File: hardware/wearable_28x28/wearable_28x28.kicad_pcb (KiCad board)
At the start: 4 copper layers, 61.2 x 61.2 mm, 784 parts

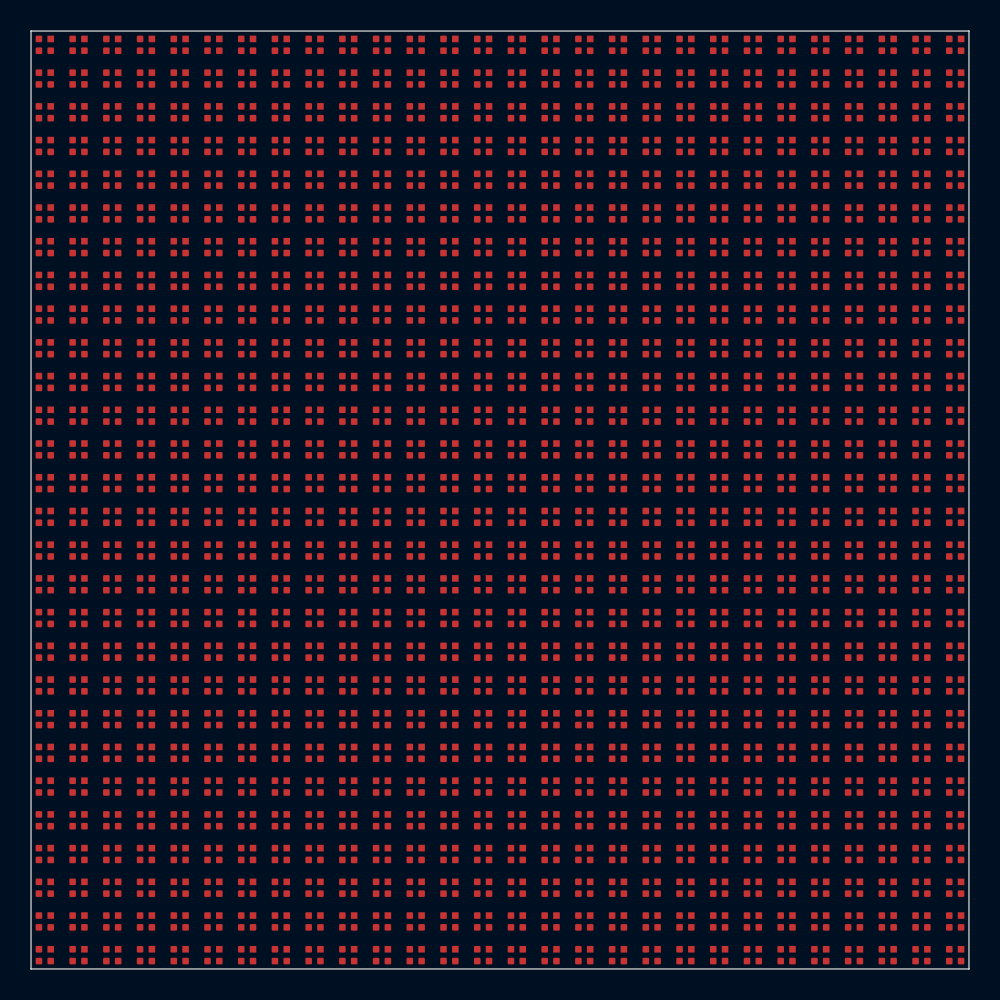
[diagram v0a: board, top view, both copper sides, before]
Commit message: Promote verified matrix routing and release gates
Co-authored-by: illiapliukhin <illiapliukhin@users.noreply.github.com>
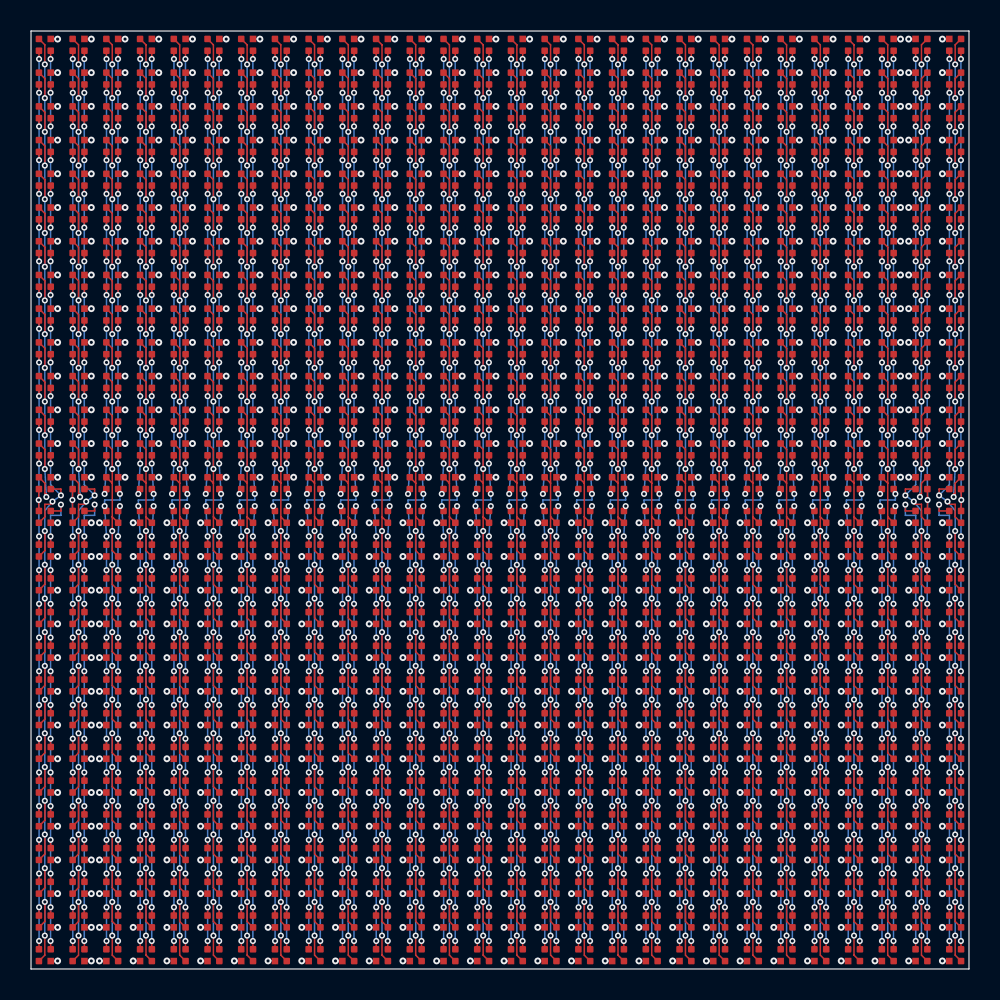
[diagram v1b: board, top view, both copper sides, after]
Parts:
- turned D111 to 90 degrees
- turned D112 to 90 degrees
- turned D139 to 90 degrees
- turned D140 to 90 degrees
- turned D167 to 90 degrees
- turned D168 to 90 degrees
- turned D195 to 90 degrees
- turned D196 to 90 degrees
- turned D223 to 90 degrees
- turned D224 to 90 degrees
- turned D251 to 90 degrees
- turned D252 to 90 degrees
- turned D27 to 90 degrees
- turned D279 to 90 degrees
- turned D28 to 90 degrees
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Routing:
- net COL_B_14: track 0.00 -> 105.2 mm, vias 0 -> 26
- net COL_B_18: track 0.00 -> 105.2 mm, vias 0 -> 26
- net COL_B_09: track 0.00 -> 105.2 mm, vias 0 -> 26
- net COL_B_20: track 0.00 -> 105.2 mm, vias 0 -> 26
- net COL_B_05: track 0.00 -> 105.2 mm, vias 0 -> 26
- net COL_B_25: track 0.00 -> 105.2 mm, vias 0 -> 26
- net COL_B_23: track 0.00 -> 105.2 mm, vias 0 -> 26
- net COL_B_15: track 0.00 -> 105.2 mm, vias 0 -> 26
- net COL_B_13: track 0.00 -> 105.2 mm, vias 0 -> 26
- net COL_B_12: track 0.00 -> 105.2 mm, vias 0 -> 26
- net COL_B_11: track 0.00 -> 105.2 mm, vias 0 -> 26
- net COL_B_10: track 0.00 -> 105.2 mm, vias 0 -> 26
- net COL_B_03: track 0.00 -> 105.2 mm, vias 0 -> 26
- net COL_B_04: track 0.00 -> 105.2 mm, vias 0 -> 26
- net COL_B_07: track 0.00 -> 105.2 mm, vias 0 -> 26
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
